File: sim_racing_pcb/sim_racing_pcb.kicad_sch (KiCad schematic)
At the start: 21 parts, among them J1 Conn_02x04_Socket, U1 A1302KUA-T, U2 A1302KUA-T, U3 LM358, U4 LM1117MP-3.3, U5 LM7805_TO220, U6 Pico

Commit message: codigo de relleno usb lib en C
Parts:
- removed C1, C2: 10uF, Capacitor_THT:CP_Radial_D5.0mm_P2.50mm, symbol Device:C_Polarized
- removed C3: 0.33uF, Capacitor_THT:C_Disc_D3.0mm_W2.0mm_P2.50mm, symbol Device:C
- removed C4: 0.1uF, Capacitor_THT:C_Disc_D3.0mm_W2.0mm_P2.50mm, symbol Device:C
- removed J1: Conn_02x04_Socket, Connector_PinHeader_2.54mm:PinHeader_2x04_P2.54mm_Vertical, symbol Connector:Conn_01x08_Socket
- removed R10, R4, R5: 10k, Resistor_THT:R_Axial_DIN0207_L6.3mm_D2.5mm_P10.16mm_Horizontal, symbol Device:R
- removed R2, R8: 2,2k, Resistor_THT:R_Axial_DIN0207_L6.3mm_D2.5mm_P10.16mm_Horizontal, symbol Device:R
- removed R3, R7, R9: 1k, Resistor_THT:R_Axial_DIN0207_L6.3mm_D2.5mm_P10.16mm_Horizontal, symbol Device:R
- removed R6: 4,7k, Resistor_THT:R_Axial_DIN0207_L6.3mm_D2.5mm_P10.16mm_Horizontal, symbol Device:R
- removed U1, U2: A1302KUA-T, Connector_PinHeader_2.54mm:PinHeader_1x03_P2.54mm_Vertical, symbol Sensor_Magnetic:A1302KUA-T
- removed U3: LM358, Package_DIP:DIP-8_W10.16mm_LongPads, symbol Amplifier_Operational:LM358
- removed U4: LM1117MP-3.3, Package_TO_SOT_SMD:SOT-223-3_TabPin2, symbol Regulator_Linear:LM1117MP-3.3
- removed U5: LM7805_TO220, Package_TO_SOT_THT:TO-220-3_Vertical, symbol Regulator_Linear:LM7805_TO220
- added H1, H2, H3, H4: MountingHole, MountingHole:MountingHole_4.3mm_M4_DIN965, symbol Mechanical:MountingHole
- added J1: Pedales MicroUsb, Connector_PinHeader_2.54mm:PinHeader_1x05_P2.54mm_Vertical, symbol Connector:Conn_01x05_Pin
- added J10: AS5600_POW, Connector_PinHeader_2.54mm:PinHeader_1x03_P2.54mm_Vertical, symbol Connector:Conn_01x03_Pin
- added J11: Conn_01x08_Pin, Connector_PinHeader_2.54mm:PinHeader_1x08_P2.54mm_Vertical, symbol Connector:Conn_01x08_Pin
- added J12, J13: Conn_01x02_Pin, Connector_PinHeader_2.54mm:PinHeader_1x02_P2.54mm_Vertical, symbol Connector:Conn_01x02_Pin
- added J2: Paddle_Shift_R, Connector_Molex:Molex_SL_171971-0002_1x02_P2.54mm_Vertical, symbol Connector:Conn_01x02_Pin
- added J3: Paddle_Shift_L, Connector_Molex:Molex_SL_171971-0002_1x02_P2.54mm_Vertical, symbol Connector:Conn_01x02_Pin
- added J4: Conn_02x04_Odd_Even, Connector_PinHeader_2.54mm:PinHeader_2x04_P2.54mm_Vertical, symbol Connector_Generic:Conn_02x04_Odd_Even
- added J5: Leds, Connector_PinHeader_2.54mm:PinHeader_1x03_P2.54mm_Vertical, symbol Connector:Conn_01x03_Pin
- added J6: AS5600, Connector_PinHeader_2.54mm:PinHeader_1x05_P2.54mm_Vertical, symbol Connector:Conn_01x05_Pin
- added J8: Encoder - DER, Connector_PinHeader_2.54mm:PinHeader_1x05_P2.54mm_Vertical, symbol Connector:Conn_01x05_Pin
- added J9: Encoder - MID, Connector_PinHeader_2.54mm:PinHeader_1x05_P2.54mm_Vertical, symbol Connector:Conn_01x05_Pin
- R1: value 1k -> 330
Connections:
- net Hall_1 is gone; now on net LEDS: R1.1
- net +3V3: now also U6.36 (3V3), J1.1 (Pin_1), J10.3 (Pin_3), J11.1 (Pin_1), J8.4 (Pin_4), J9.4 (Pin_4)
- net +5V: now also U6.40 (VBUS), J10.1 (Pin_1), J5.1 (Pin_1)
- net A0-Acc: now also U6.31 (GPIO26_ADC0), J1.3 (Pin_3)
- net A1-Brk: now also U6.32 (GPIO27_ADC1), J1.2 (Pin_2)
- net DIR: now also U6.25 (GPIO19), J6.2 (Pin_2)
- net GND: now also U6.13 (GND), U6.18 (GND), U6.23 (GND), U6.28 (GND), U6.3 (GND), U6.33 (AGND), U6.38 (GND), U6.8 (GND), J1.5 (Pin_5), J11.2 (Pin_2), J12.1 (Pin_1), J12.2 (Pin_2), J13.1 (Pin_1), J13.2 (Pin_2), J2.2 (Pin_2), J3.2 (Pin_2), J4.1 (Pin_1), J4.3 (Pin_3), J4.5 (Pin_5), J4.7 (Pin_7), J5.3 (Pin_3), J6.5 (Pin_5), J8.5 (Pin_5), J9.5 (Pin_5)
- net SCL: now also U6.27 (GPIO21), J6.4 (Pin_4)
- net SDA: now also U6.26 (GPIO20), J6.3 (Pin_3)
- net at R1.2: now also J5.2 (Pin_2)
- net Shifter_mec_L: now reaches U6.1 (GPIO0)
- net Shifter_mec_L: now also J3.1 (Pin_1)
- net DIS - LED: now reaches U6.10 (GPIO7)
- net DIS - LED: now also J11.8 (Pin_8)
- net DIS - DC: now reaches U6.11 (GPIO8)
- net DIS - DC: now also J11.5 (Pin_5)
- net BTN 1: now reaches U6.12 (GPIO9)
- net BTN 1: now also J4.2 (Pin_2)
- net BTN 2: now reaches U6.14 (GPIO10)
- net BTN 2: now also J4.4 (Pin_4)
- net BTN 3: now reaches U6.15 (GPIO11)
- net BTN 3: now also J4.6 (Pin_6)
- net BTN 4: now reaches U6.16 (GPIO12)
- net BTN 4: now also J4.8 (Pin_8)
- net CLK - MID: now reaches U6.17 (GPIO13)
- net CLK - MID: now also J9.1 (Pin_1)
- net SW - MID: now reaches U6.19 (GPIO14)
- net SW - MID: now also J9.3 (Pin_3)
- net DIS - CS: now reaches U6.2 (GPIO1)
- net DIS - CS: now also J11.3 (Pin_3)
- net DT - MID: now reaches U6.20 (GPIO15)
- net DT - MID: now also J9.2 (Pin_2)
- net SW - DER: now reaches U6.21 (GPIO16)
- net SW - DER: now also J8.3 (Pin_3)
- net DT - DER: now reaches U6.22 (GPIO17)
- net DT - DER: now also J8.2 (Pin_2)
- net CLK - DER: now reaches U6.24 (GPIO18)
- net CLK - DER: now also J8.1 (Pin_1)
- net LEDS: now reaches U6.29 (GPIO22)
- net DIS - RST: now reaches U6.4 (GPIO2)
- net DIS - RST: now also J11.4 (Pin_4)
- net DIS - MOSI: now reaches U6.5 (GPIO3)
- net DIS - MOSI: now also J11.6 (Pin_6)
- net Shifter_mec_R: now reaches U6.7 (GPIO5)
- net Shifter_mec_R: now also J2.1 (Pin_1)
- net DIS - CLK: now reaches U6.9 (GPIO6)
- net DIS - CLK: now also J11.7 (Pin_7)
- new net AS5600: J10.2 (Pin_2), J6.1 (Pin_1)
- no-connect marks 0 -> 9
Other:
- note added: "Botones y switches"
- moved on the sheet: U6

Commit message: minor changes to pcb
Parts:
- added J7: USB_OTG, Connector_USB:USB_Micro-AB_Molex_47590-0001, symbol Connector:USB_OTG
- H1, H2, H3, H4: footprint MountingHole:MountingHole_4.3mm_M4_DIN965 -> MountingHole:MountingHole_3.2mm_M3_DIN965
- J11: value Conn_01x08_Pin -> Display TFT
- J2, J3: footprint Connector_Molex:Molex_SL_171971-0002_1x02_P2.54mm_Vertical -> Connector_Molex:Molex_KK-254_AE-6410-02A_1x02_P2.54mm_Vertical
- R1: footprint Resistor_THT:R_Axial_DIN0207_L6.3mm_D2.5mm_P10.16mm_Horizontal -> Resistor_THT:R_Axial_DIN0207_L6.3mm_D2.5mm_P15.24mm_Horizontal
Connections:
- net +3V3: now also J7.1 (VBUS)
- net A0-Acc: now also J1.4 (Pin_4), J7.4 (ID); no longer J1.3 (Pin_3)
- net A1-Brk: now also J1.3 (Pin_3), J7.2 (D-); no longer J1.2 (Pin_2)
- net CLK - MID: now also U6.20 (GPIO15); no longer U6.17 (GPIO13)
- net DT - MID: now also U6.19 (GPIO14); no longer U6.20 (GPIO15)
- net GND: now also J2.1 (Pin_1), J3.1 (Pin_1), J7.5 (GND), J7.6 (Shield); no longer J2.2 (Pin_2), J3.2 (Pin_2)
- net SW - MID: now also U6.17 (GPIO13); no longer U6.19 (GPIO14)
- net Shifter_mec_L: now also J3.2 (Pin_2); no longer J3.1 (Pin_1)
- net Shifter_mec_R: now also J2.2 (Pin_2); no longer J2.1 (Pin_1)
- net A2-Clutch: now reaches U6.34 (GPIO28_ADC2)
- net A2-Clutch: now also J1.2 (Pin_2)
- no-connect marks 9 -> 7

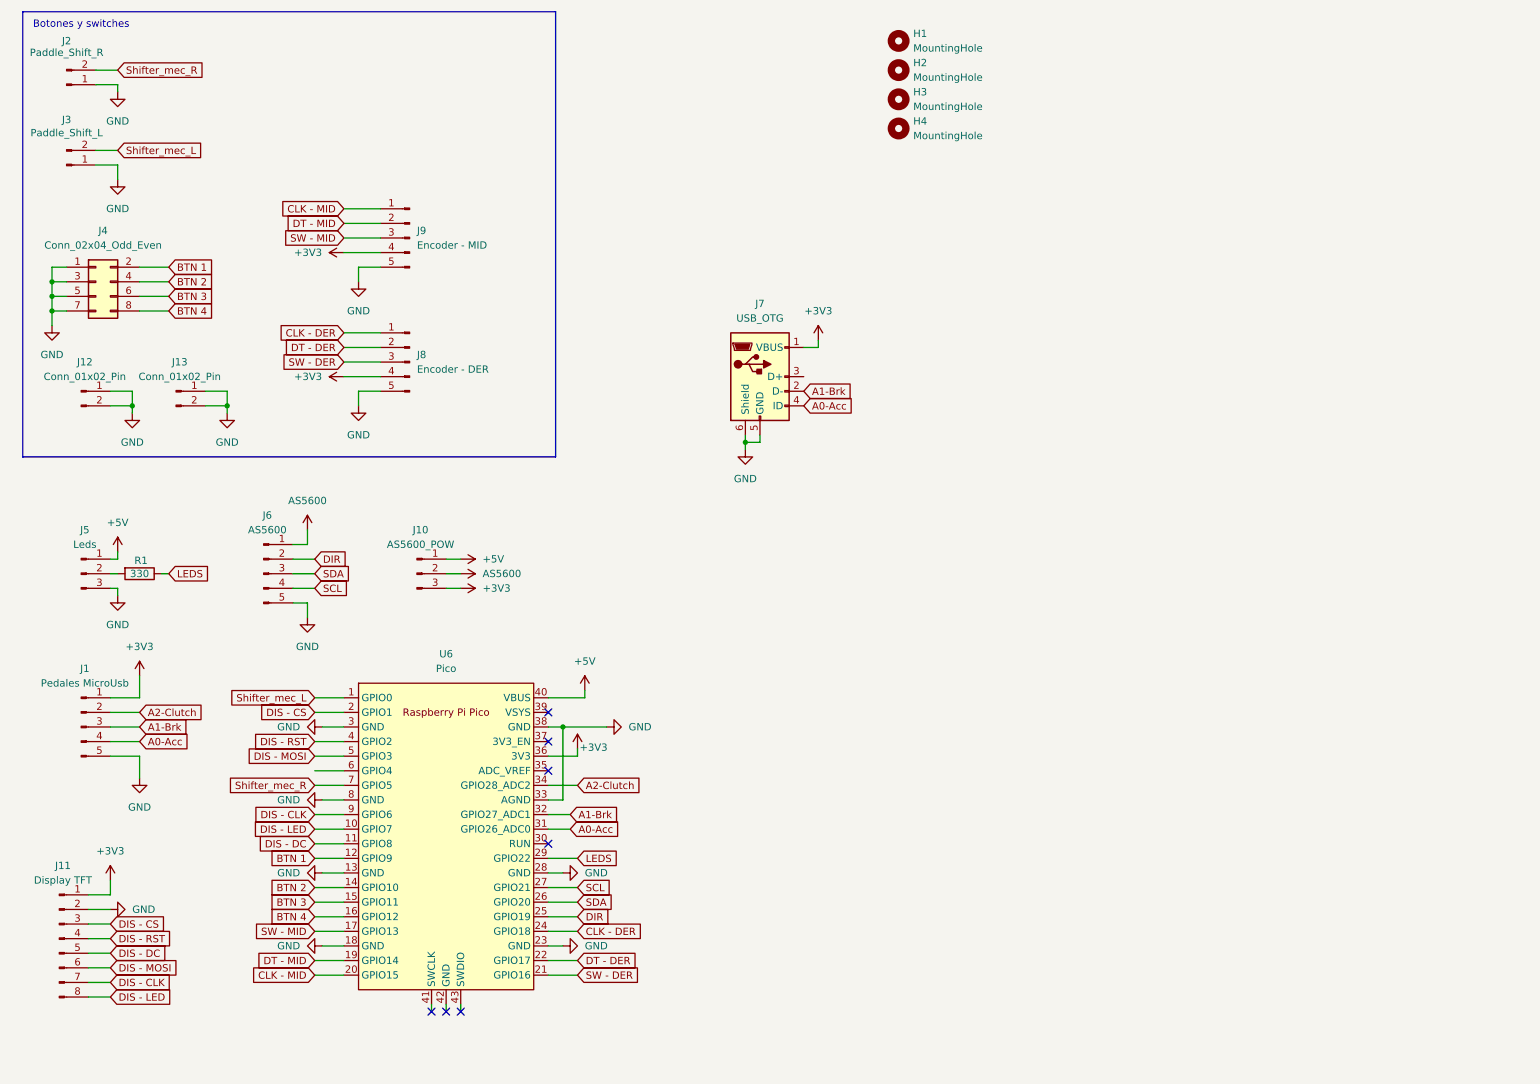
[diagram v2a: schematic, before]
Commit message: modify pcb display placement
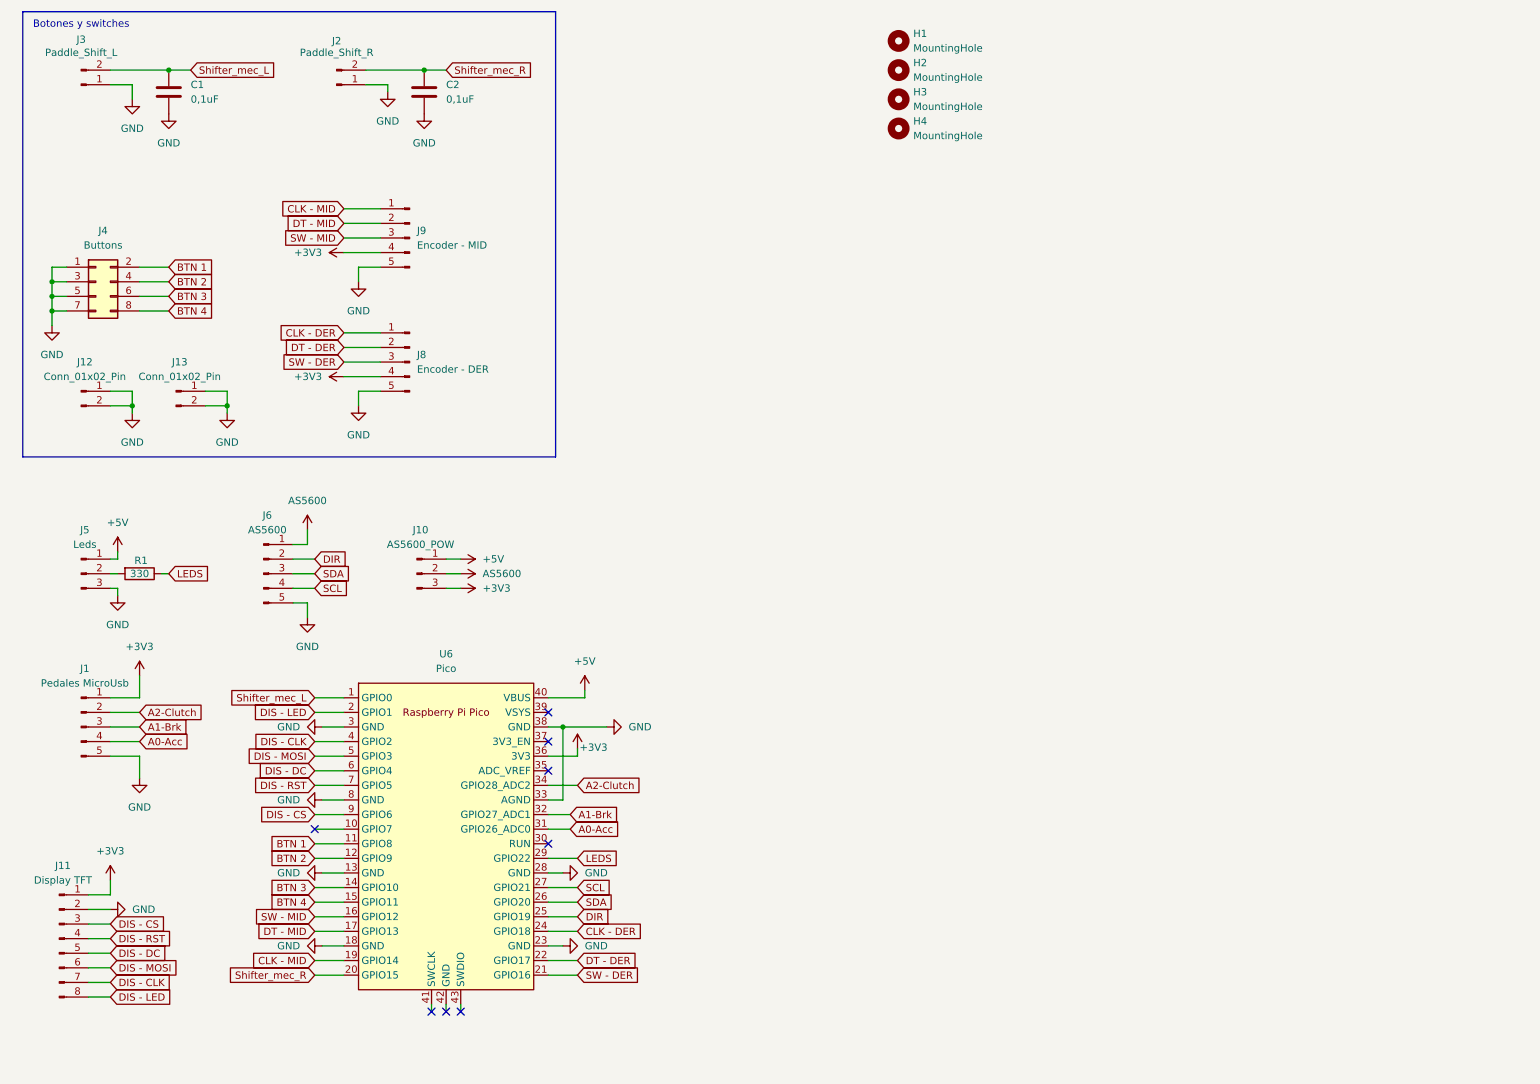
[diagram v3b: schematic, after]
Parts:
- removed J7: USB_OTG, Connector_USB:USB_Micro-AB_Molex_47590-0001, symbol Connector:USB_OTG
- added C1, C2: 0,1uF, Capacitor_THT:C_Disc_D3.4mm_W2.1mm_P2.50mm, symbol Device:C
- J4: value Conn_02x04_Odd_Even -> Buttons
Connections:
- net BTN 1: now also U6.11 (GPIO8); no longer U6.12 (GPIO9)
- net BTN 2: now also U6.12 (GPIO9); no longer U6.14 (GPIO10)
- net BTN 3: now also U6.14 (GPIO10); no longer U6.15 (GPIO11)
- net BTN 4: now also U6.15 (GPIO11); no longer U6.16 (GPIO12)
- net CLK - MID: now also U6.19 (GPIO14); no longer U6.20 (GPIO15)
- net DIS - CLK: now also U6.4 (GPIO2); no longer U6.9 (GPIO6)
- net DIS - CS: now also U6.9 (GPIO6); no longer U6.2 (GPIO1)
- net DIS - DC: now also U6.6 (GPIO4); no longer U6.11 (GPIO8)
- net DIS - LED: now also U6.2 (GPIO1); no longer U6.10 (GPIO7)
- net DIS - RST: now also U6.7 (GPIO5); no longer U6.4 (GPIO2)
- net DT - MID: now also U6.17 (GPIO13); no longer U6.19 (GPIO14)
- net GND: now also C1.2, C2.2
- net SW - MID: now also U6.16 (GPIO12); no longer U6.17 (GPIO13)
- net Shifter_mec_L: now also C1.1
- net Shifter_mec_R: now also U6.20 (GPIO15), C2.1; no longer U6.7 (GPIO5)
- no-connect marks 7 -> 8
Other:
- moved on the sheet: J2, J3

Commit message: Remove power selection for as5600 and change for molex connectors
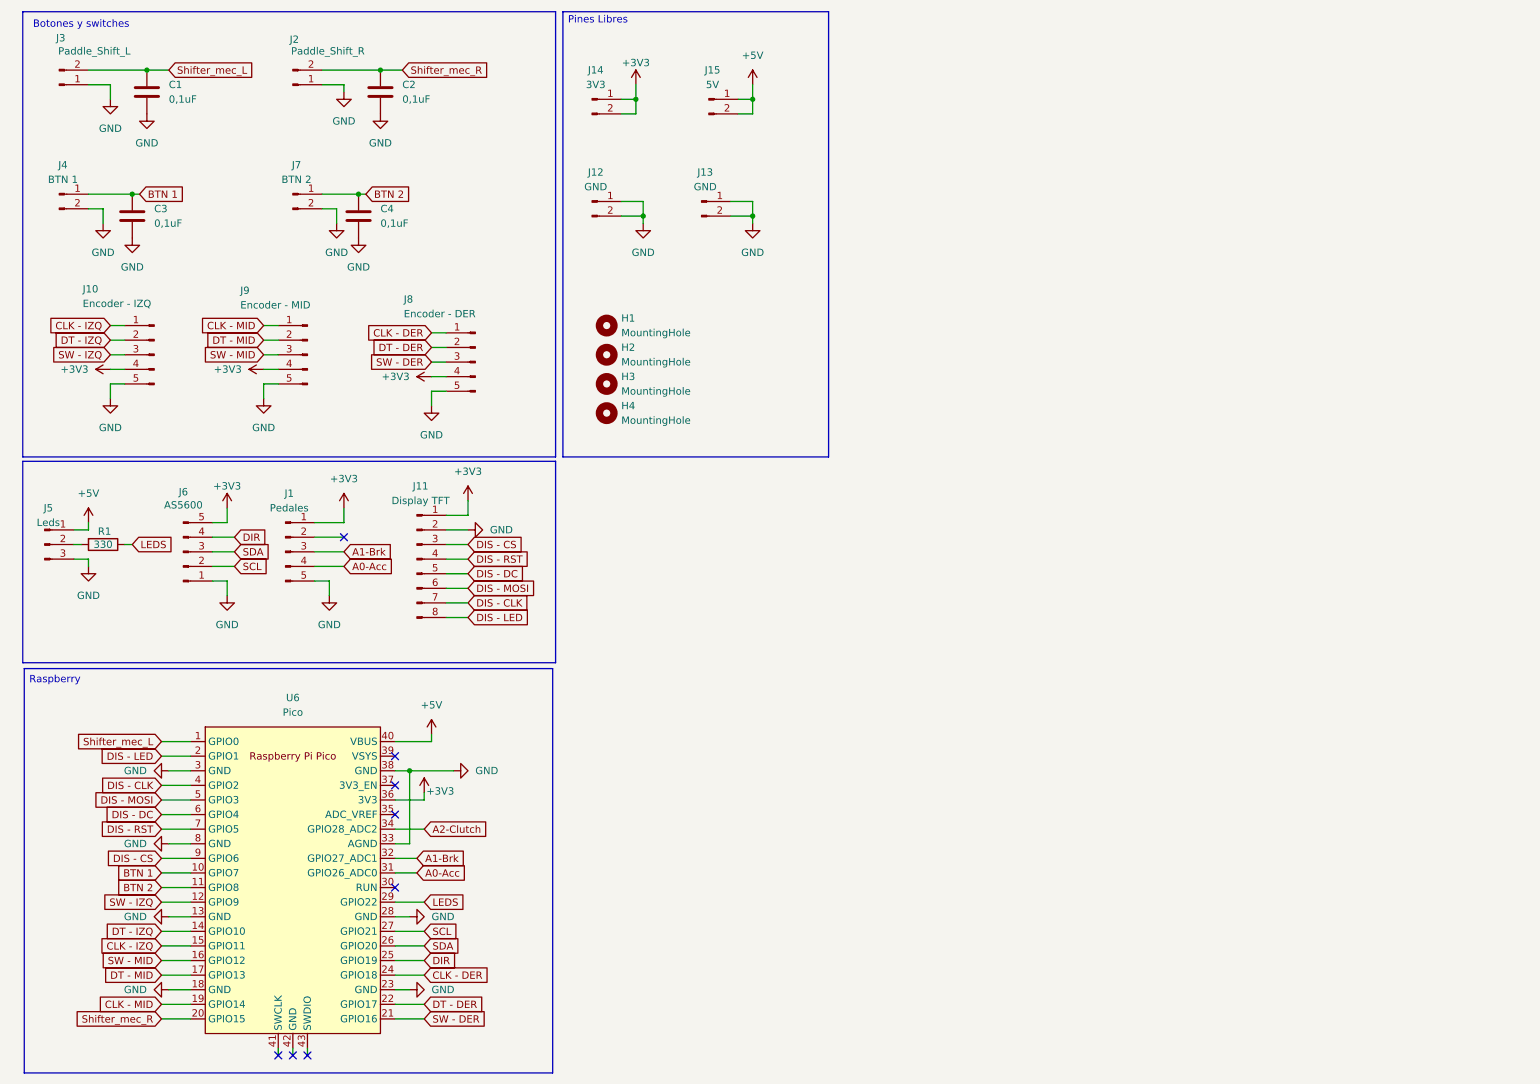
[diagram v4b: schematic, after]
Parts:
- removed J10: AS5600_POW, Connector_PinHeader_2.54mm:PinHeader_1x03_P2.54mm_Vertical, symbol Connector:Conn_01x03_Pin
- removed J4: Buttons, Connector_PinHeader_2.54mm:PinHeader_2x04_P2.54mm_Vertical, symbol Connector_Generic:Conn_02x04_Odd_Even
- added C3, C4: 0,1uF, Capacitor_THT:C_Disc_D3.4mm_W2.1mm_P2.50mm, symbol Device:C
- added J10: Encoder - IZQ, Connector_Molex:Molex_KK-254_AE-6410-05A_1x05_P2.54mm_Vertical, symbol Connector:Conn_01x05_Pin
- added J14: 3V3, Connector_PinHeader_2.54mm:PinHeader_1x02_P2.54mm_Vertical, symbol Connector:Conn_01x02_Pin
- added J15: 5V, Connector_PinHeader_2.54mm:PinHeader_1x02_P2.54mm_Vertical, symbol Connector:Conn_01x02_Pin
- added J4: BTN 1, Connector_Molex:Molex_KK-254_AE-6410-02A_1x02_P2.54mm_Vertical, symbol Connector:Conn_01x02_Pin
- added J7: BTN 2, Connector_Molex:Molex_KK-254_AE-6410-02A_1x02_P2.54mm_Vertical, symbol Connector:Conn_01x02_Pin
- J1: value Pedales MicroUsb -> Pedales; footprint Connector_PinHeader_2.54mm:PinHeader_1x05_P2.54mm_Vertical -> Connector_Molex:Molex_KK-254_AE-6410-05A_1x05_P2.54mm_Vertical
- J11: footprint Connector_PinHeader_2.54mm:PinHeader_1x08_P2.54mm_Vertical -> Connector_Molex:Molex_KK-254_AE-6410-08A_1x08_P2.54mm_Vertical
- J12, J13: value Conn_01x02_Pin -> GND
- J5: footprint Connector_PinHeader_2.54mm:PinHeader_1x03_P2.54mm_Vertical -> Connector_Molex:Molex_KK-254_AE-6410-03A_1x03_P2.54mm_Vertical
- J6, J8, J9: footprint Connector_PinHeader_2.54mm:PinHeader_1x05_P2.54mm_Vertical -> Connector_Molex:Molex_KK-254_AE-6410-05A_1x05_P2.54mm_Vertical
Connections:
- net AS5600 is gone; now on net GND: J6.1 (Pin_1)
- net +3V3: now also J6.5 (Pin_5), J10.4 (Pin_4), J14.1 (Pin_1), J14.2 (Pin_2)
- net +5V: now also J15.1 (Pin_1), J15.2 (Pin_2)
- net A2-Clutch: no longer J1.2 (Pin_2)
- net BTN 1: now also U6.10 (GPIO7), C3.1, J4.1 (Pin_1); no longer U6.11 (GPIO8)
- net BTN 2: now also U6.11 (GPIO8), C4.1, J7.1 (Pin_1); no longer U6.12 (GPIO9)
- net DIR: now also J6.4 (Pin_4); no longer J6.2 (Pin_2)
- net GND: now also C3.2, C4.2, J10.5 (Pin_5), J4.2 (Pin_2), J7.2 (Pin_2); no longer J6.5 (Pin_5)
- net SCL: now also J6.2 (Pin_2); no longer J6.4 (Pin_4)
- net BTN 3 renamed DT - IZQ
- net DT - IZQ: now also J10.2 (Pin_2)
- net BTN 4 renamed CLK - IZQ
- net CLK - IZQ: now also J10.1 (Pin_1)
- new net SW - IZQ: J10.3 (Pin_3), U6.12 (GPIO9)
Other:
- note added: "Pines Libres"
- note added: "Raspberry"
- moved on the sheet: C1, C2, H1, H2, H3, H4, J1, J11, J12, J13, J2, J3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

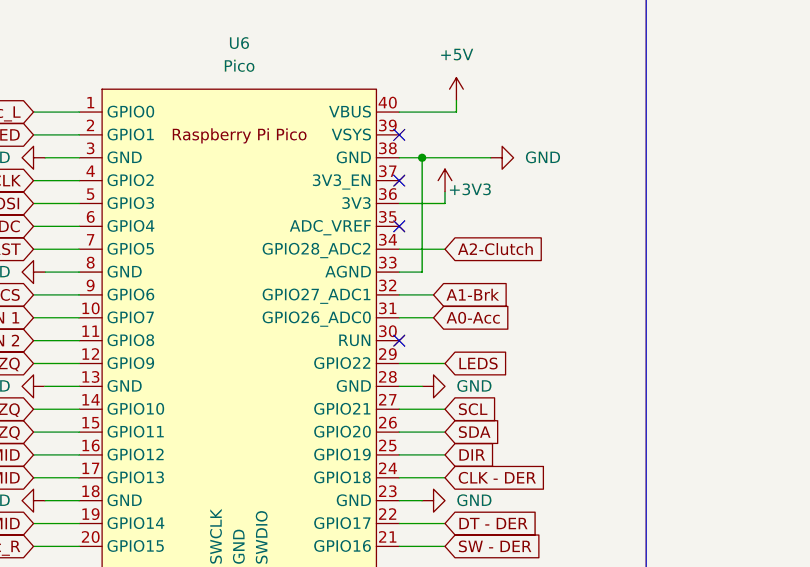
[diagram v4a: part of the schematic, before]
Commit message: modify position of buttons
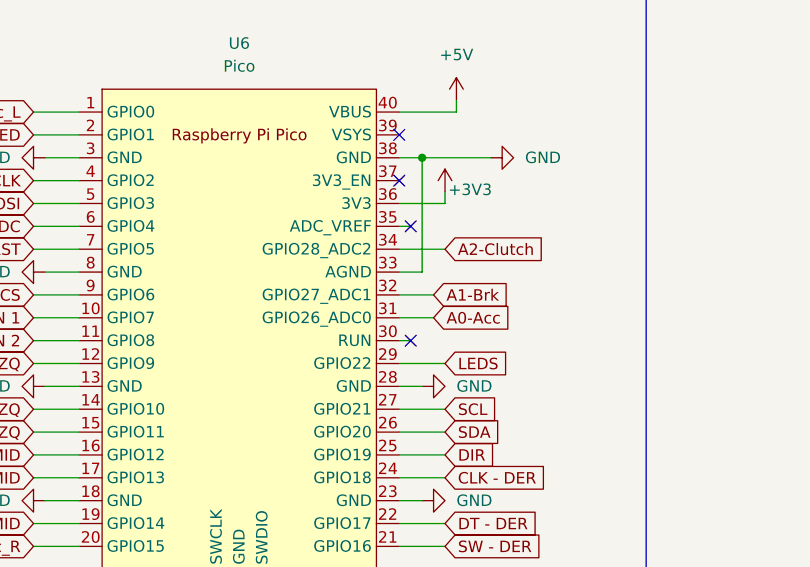
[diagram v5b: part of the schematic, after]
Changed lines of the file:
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@@
 	)
 	(no_connect
-		(at 77.47 152.4)
+		(at 78.74 152.4)
 	)
 	(no_connect
-		(at 77.47 165.1)
+		(at 78.74 165.1)
 	)
 	(wire
@@
 	(wire
 		(pts
+			(xy 78.74 152.4) (xy 77.47 152.4)
+		)
+		(stroke
+			(width 0)
+			(type default)
+		)
+	)
+	(wire
+		(pts
 			(xy 82.55 175.26) (xy 77.47 175.26)
 		)
@@
 		)
 		(stroke
+			(width 0)
+			(type default)
+		)
+	)
+	(wire
+		(pts
+			(xy 78.74 165.1) (xy 77.47 165.1)
+		)
+		(stroke
